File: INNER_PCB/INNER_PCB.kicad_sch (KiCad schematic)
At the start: 0 parts

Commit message: finished second PCB
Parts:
- added C3: 100nF, Capacitor_SMD:C_0402_1005Metric, symbol Device:C
- added J1: Conn_01x03, Connector_PinHeader_2.54mm:PinHeader_1x03_P2.54mm_Vertical, symbol Connector_Generic:Conn_01x03
- added J2: Conn_01x02, Connector_PinHeader_2.54mm:PinHeader_1x02_P2.54mm_Vertical, symbol Connector_Generic:Conn_01x02
- added R1: 1k, Resistor_SMD:R_0402_1005Metric, symbol Device:R
- added TP1, TP2, TP3, TP4: TestPoint, TestPoint:TestPoint_Pad_3.0x3.0mm, symbol Connector:TestPoint
- added U2: CH32V003FxUx, Package_DFN_QFN:QFN-20-1EP_3x3mm_P0.4mm_EP1.65x1.65mm_ThermalVias, symbol MCU_WCH_RiscV:CH32V003FxUx
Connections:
- new net +3.7V: C3.1, J1.2 (Pin_2), J2.2 (Pin_2), R1.1, TP4.1, U2.6 (VDD)
- new net GND: C3.2, J1.1 (Pin_1), J2.1 (Pin_1), TP1.1, TP2.1, U2.21 (VSS), U2.4 (VSS)
- new net LED_DOUT: TP3.1, U2.7 (PC0)
- new net PA1: U2.2 (PA1)
- new net PA2: U2.3 (PA2)
- new net PC0: U2.10 (PC3)
- new net PC1: U2.8 (PC1)
- new net PC2: U2.9 (PC2)
- new net PC4: U2.11 (PC4)
- new net PC5: U2.12 (PC5)
- new net PC6: U2.13 (PC6)
- new net PC7: U2.14 (PC7)
- new net PD0: U2.5 (PD0)
- new net PD2: U2.16 (PD2)
- new net PD3: U2.17 (PD3)
- new net PD4: U2.18 (PD4)
- new net PD5: U2.19 (PD5)
- new net PD6: U2.20 (PD6)
- new net PD7: U2.1 (PD7)
- new net SWIO: J1.3 (Pin_3), R1.2, U2.15 (PD1)

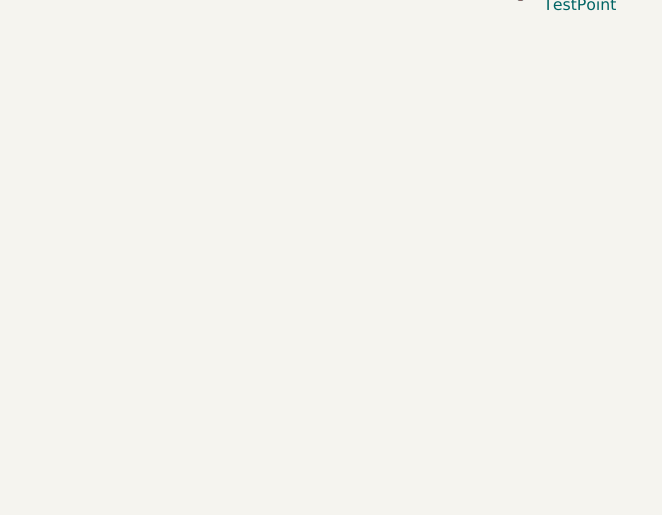
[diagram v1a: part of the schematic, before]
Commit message: added the second side to the second PCB
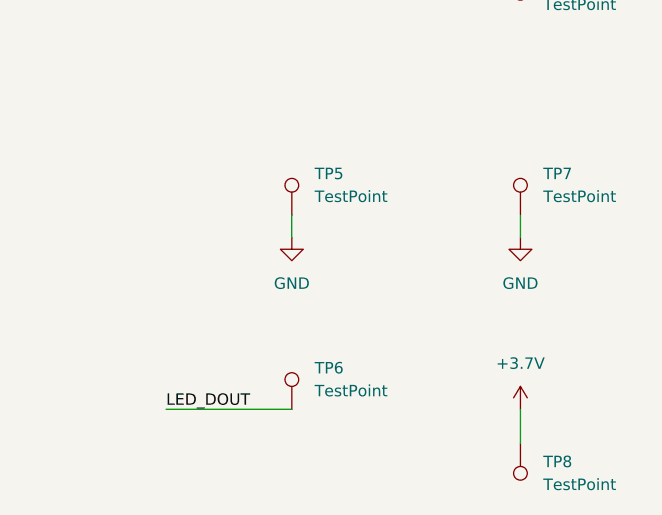
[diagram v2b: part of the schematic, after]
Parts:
- added TP5, TP6, TP7, TP8: TestPoint, TestPoint:TestPoint_Pad_3.0x3.0mm, symbol Connector:TestPoint
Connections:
- net +3.7V: now also TP8.1
- net GND: now also TP5.1, TP7.1
- net LED_DOUT: now also TP6.1

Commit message: update
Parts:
- added D1, D10, D11, D12, D13, D14, D15, D16, D2, D3, D4, D5, D6, D7, D8, D9: KT-0603Y, LED_SMD:LED_0603_1608Metric, symbol Device:LED
- added R10, R11, R12, R13, R14, R15, R16, R17, R2, R3, R4, R5, R6, R7, R8, R9: 2k, Resistor_SMD:R_0402_1005Metric, symbol Device:R
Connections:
- net +3.7V: now also R10.1, R11.1, R12.1, R13.1, R14.1, R15.1, R16.1, R17.1, R2.1, R3.1, R4.1, R5.1, R6.1, R7.1, R8.1, R9.1
- net GND: now also D1.1 (K), D10.1 (K), D11.1 (K), D12.1 (K), D13.1 (K), D14.1 (K), D15.1 (K), D16.1 (K), D2.1 (K), D3.1 (K), D4.1 (K), D5.1 (K), D6.1 (K), D7.1 (K), D8.1 (K), D9.1 (K)
- new net: D16.2 (A), R17.2
- new net: D13.2 (A), R14.2
- new net: D6.2 (A), R7.2
- new net: D14.2 (A), R15.2
- new net: D4.2 (A), R5.2
- new net: D10.2 (A), R11.2
- new net: D8.2 (A), R9.2
- new net: D7.2 (A), R8.2
- new net: D5.2 (A), R6.2
- new net: D15.2 (A), R16.2
- new net: D12.2 (A), R13.2
- new net: D11.2 (A), R12.2
- new net: D3.2 (A), R4.2
- new net: D9.2 (A), R10.2
- new net: D1.2 (A), R2.2
- new net: D2.2 (A), R3.2
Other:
- moved on the sheet: C3, J1, J2, R1, TP1, TP2, TP3, TP4, TP5, TP6, TP7, TP8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
